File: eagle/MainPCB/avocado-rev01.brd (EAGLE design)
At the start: 100 x 60 mm, 85 parts, among them J1 10118194-0001LF, J2 CON-DSUB-15-VGA, J3 0475710001, P2 CONNECTOR-15686115148922, U1 V3S, U2 AP65111A, U3 AP65111A, U4 AP65111A

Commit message: updated i2c
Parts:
- removed R31: 2k, resistor:R0603
- R27: value (none) -> 2k
- moved R27 2.00 mm to (69.0, 37.0)
- moved R28 2.00 mm to (69.0, 39.0)
- moved R29 2.00 mm to (69.0, 41.0)
- moved R30 2.00 mm to (69.0, 43.0)
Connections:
- net N$49: no longer R28.2
- net N$50: now also R28.2; no longer R29.2
- net N$51: now also R29.2; no longer R30.2
- net N$52: now also R30.2; no longer R31.2
- net N$63: no longer R31.1
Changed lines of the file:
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@@
 <attribute name="X" value="X" x="38" y="58" size="1.778" layer="27" rot="R270" display="off"/>
 </element>
-<element name="R27" library="resistor" library_urn="urn:adsk.eagle:library:348" package="R0603" package3d_urn="urn:adsk.eagle:package:26057/1" value="" x="69" y="35" smashed="yes" rot="R180">
-<attribute name="NAME" x="74.635" y="35.365" size="1.27" layer="25" rot="R180"/>
-<attribute name="VALUE" x="69.635" y="36.905" size="1.27" layer="27" rot="R180"/>
-</element>
-<element name="R28" library="resistor" library_urn="urn:adsk.eagle:library:348" package="R0603" package3d_urn="urn:adsk.eagle:package:26057/1" value="2k" x="69" y="37" smashed="yes" rot="R180">
+<element name="R27" library="resistor" library_urn="urn:adsk.eagle:library:348" package="R0603" package3d_urn="urn:adsk.eagle:package:26057/1" value="2k" x="69" y="37" smashed="yes" rot="R180">
 <attribute name="NAME" x="74.635" y="37.365" size="1.27" layer="25" rot="R180"/>
 <attribute name="VALUE" x="69.635" y="38.905" size="1.27" layer="27" rot="R180"/>
 </element>
-<element name="R29" library="resistor" library_urn="urn:adsk.eagle:library:348" package="R0603" package3d_urn="urn:adsk.eagle:package:26057/1" value="2k" x="69" y="39" smashed="yes" rot="R180">
+<element name="R28" library="resistor" library_urn="urn:adsk.eagle:library:348" package="R0603" package3d_urn="urn:adsk.eagle:package:26057/1" value="2k" x="69" y="39" smashed="yes" rot="R180">
 <attribute name="NAME" x="74.635" y="39.365" size="1.27" layer="25" rot="R180"/>
 <attribute name="VALUE" x="69.635" y="40.905" size="1.27" layer="27" rot="R180"/>
 </element>
-<element name="R30" library="resistor" library_urn="urn:adsk.eagle:library:348" package="R0603" package3d_urn="urn:adsk.eagle:package:26057/1" value="2k" x="69" y="41" smashed="yes" rot="R180">
+<element name="R29" library="resistor" library_urn="urn:adsk.eagle:library:348" package="R0603" package3d_urn="urn:adsk.eagle:package:26057/1" value="2k" x="69" y="41" smashed="yes" rot="R180">
 <attribute name="NAME" x="74.635" y="41.365" size="1.27" layer="25" rot="R180"/>
 <attribute name="VALUE" x="69.635" y="42.905" size="1.27" layer="27" rot="R180"/>
 </element>
-<element name="R31" library="resistor" library_urn="urn:adsk.eagle:library:348" package="R0603" package3d_urn="urn:adsk.eagle:package:26057/1" value="2k" x="69" y="43" smashed="yes" rot="R180">
+<element name="R30" library="resistor" library_urn="urn:adsk.eagle:library:348" package="R0603" package3d_urn="urn:adsk.eagle:package:26057/1" value="2k" x="69" y="43" smashed="yes" rot="R180">
 <attribute name="NAME" x="74.635" y="43.365" size="1.27" layer="25" rot="R180"/>
 <attribute name="VALUE" x="69.635" y="44.905" size="1.27" layer="27" rot="R180"/>
@@
 <contactref element="TP5" pad="1"/>
 <contactref element="R27" pad="2"/>
-<contactref element="R28" pad="2"/>
 <wire x1="56.363959375" y1="34.384059375" x2="56" y2="58" width="0" layer="19" extent="1-1"/>
-<wire x1="68.15" y1="35" x2="56.363959375" y2="34.384059375" width="0" layer="19" extent="1-1"/>
-<wire x1="68.15" y1="37" x2="68.15" y2="35" width="0" layer="19" extent="1-1"/>
+<wire x1="68.15" y1="37" x2="56.363959375" y2="34.384059375" width="0" layer="19" extent="1-1"/>
 </signal>
 <signal name="N$50">
 <contactref element="U1" pad="46"/>
 <contactref element="TP6" pad="1"/>
-<contactref element="R29" pad="2"/>
+<contactref element="R28" pad="2"/>
 <wire x1="56.081115625" y1="34.666903125" x2="54" y2="58" width="0" layer="19" extent="1-1"/>
 <wire x1="68.15" y1="39" x2="56.081115625" y2="34.666903125" width="0" layer="19" extent="1-1"/>
@@
 <contactref element="U1" pad="48"/>
 <contactref element="TP7" pad="1"/>
-<contactref element="R30" pad="2"/>
+<contactref element="R29" pad="2"/>
 <wire x1="55.51543125" y1="35.2325875" x2="52" y2="58" width="0" layer="19" extent="1-1"/>
 <wire x1="68.15" y1="41" x2="55.51543125" y2="35.2325875" width="0" layer="19" extent="1-1"/>
@@
 <contactref element="U1" pad="49"/>
 <contactref element="TP8" pad="1"/>
-<contactref element="R31" pad="2"/>
+<contactref element="R30" pad="2"/>
 <wire x1="55.2325875" y1="35.51543125" x2="50" y2="58" width="0" layer="19" extent="1-1"/>
 <wire x1="68.15" y1="43" x2="55.2325875" y2="35.51543125" width="0" layer="19" extent="1-1"/>
@@
 <signal name="N$63">
 <contactref element="R27" pad="1"/>
+<contactref element="R30" pad="1"/>
 <contactref element="R28" pad="1"/>
-<contactref element="R31" pad="1"/>
 <contactref element="R29" pad="1"/>
-<contactref element="R30" pad="1"/>
 <wire x1="69.85" y1="41" x2="69.85" y2="43" width="0" layer="19" extent="1-1"/>
 <wire x1="69.85" y1="39" x2="69.85" y2="41" width="0" layer="19" extent="1-1"/>
 <wire x1="69.85" y1="37" x2="69.85" y2="39" width="0" layer="19" extent="1-1"/>
-<wire x1="69.85" y1="35" x2="69.85" y2="37" width="0" layer="19" extent="1-1"/>
 </signal>
 </signals>

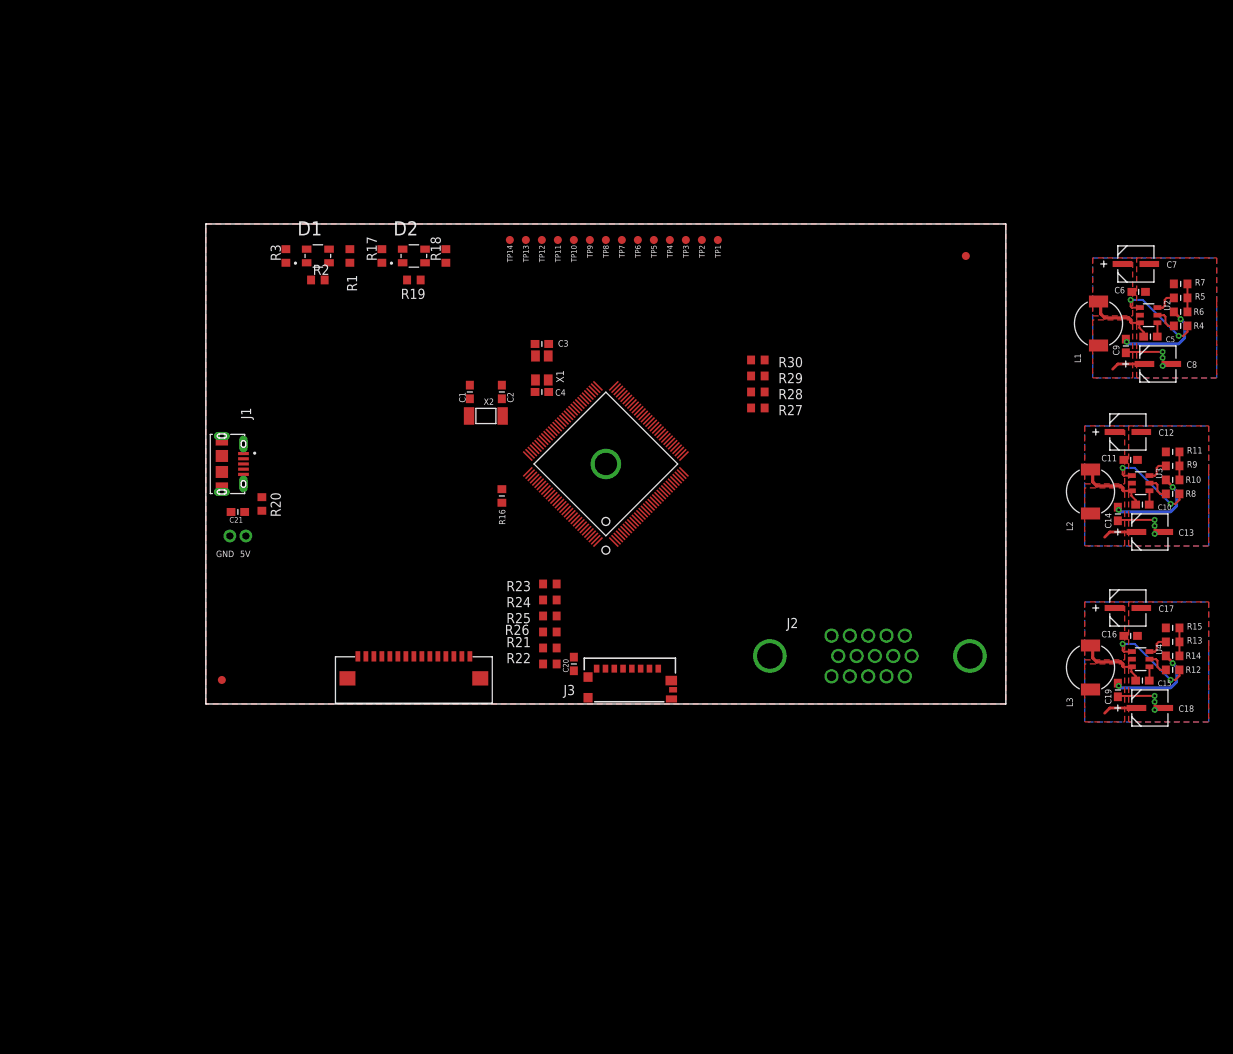
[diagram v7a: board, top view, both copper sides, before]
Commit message: connected psu in schem
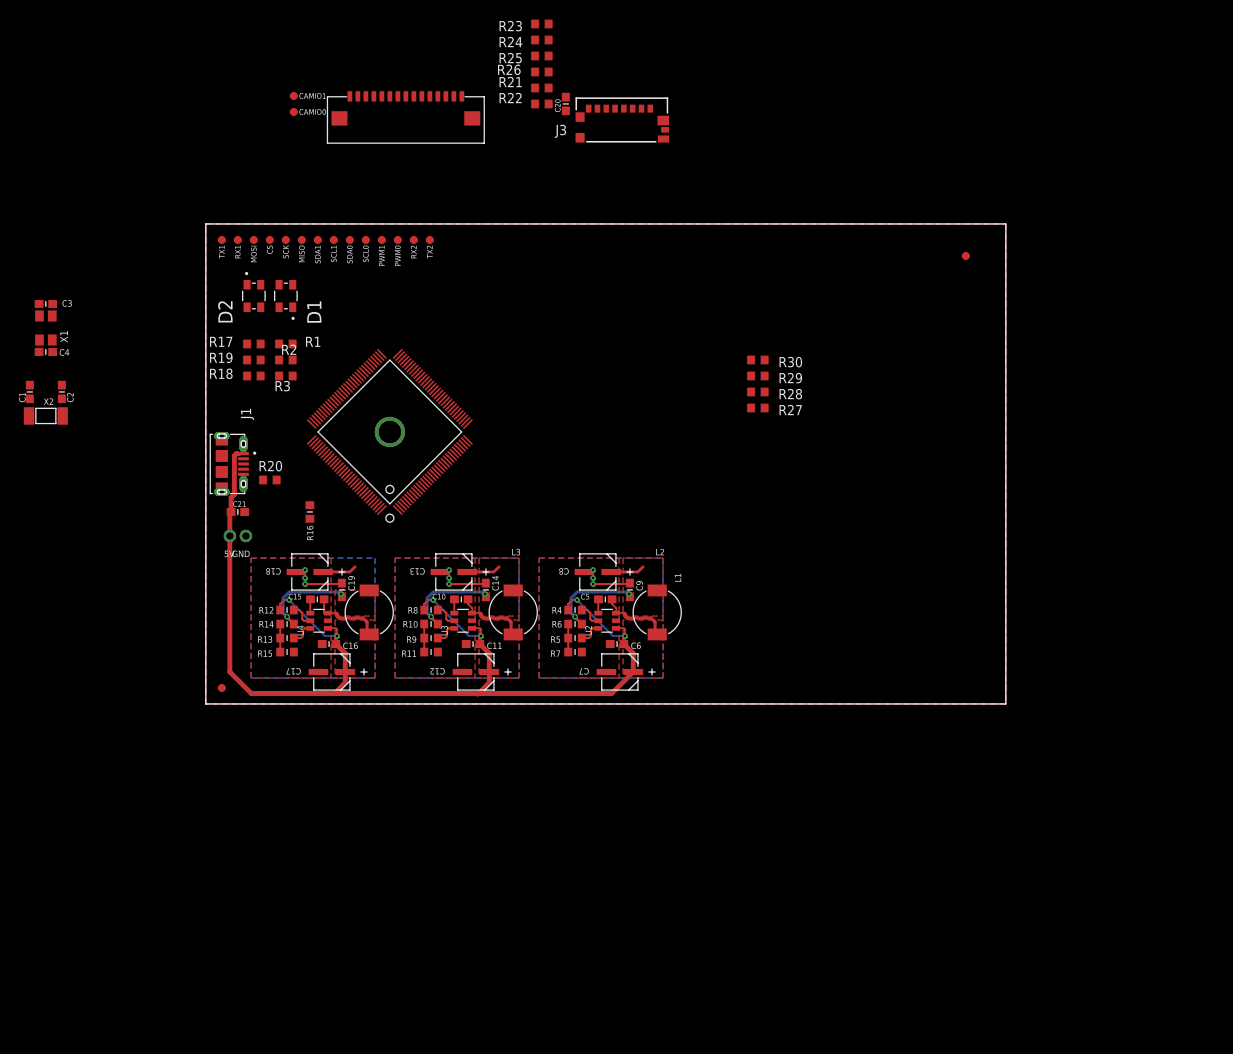
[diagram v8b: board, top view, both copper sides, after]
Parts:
- removed J2: CON-DSUB-15-VGA, m-pad-2.1:181-015-212-171
- removed TP1, TP10, TP11, TP12, TP13, TP14, TP2, TP3, TP4, TP5, TP6, TP7, TP8, TP9: TEST_TESTPOINT, marius:TEST_TESTPOINT
- added CAMIO0, CAMIO1, CS, MISO, MOSI, PWM0, PWM1, RX1, RX2, SCK, SCL0, SCL1, SDA0, SDA1, TX1, TX2: TEST_TESTPOINT, marius:TEST_TESTPOINT
- moved R12 111.0 mm to (10.2, 11.7), turned to 180 degrees
- moved R14 110.8 mm to (10.2, 9.99), turned to 180 degrees
- moved R15 110.7 mm to (10.2, 6.49), turned to 0 degrees
- moved R13 110.7 mm to (10.2, 8.24), turned to 0 degrees
- moved C18 106.4 mm to (13.0, 16.5), turned to 180 degrees
- moved C15 103.6 mm to (13.9, 13.1), turned to 0 degrees
- moved U4 102.8 mm to (14.2, 10.4), turned to 90 degrees
- moved C16 100.2 mm to (15.4, 7.49), turned to 180 degrees
- moved C17 99.8 mm to (15.8, 4.00), turned to 180 degrees
- moved C19 97.8 mm to (17.0, 14.2), turned to 90 degrees
- moved R11 96.0 mm to (28.1, 6.49), turned to 0 degrees
- moved R9 95.2 mm to (28.1, 8.24), turned to 0 degrees
- moved R10 94.4 mm to (28.1, 9.99), turned to 180 degrees
- moved R8 93.8 mm to (28.1, 11.7), turned to 180 degrees
- moved L3 90.4 mm to (20.4, 11.4), turned to 90 degrees
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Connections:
- removed net N$26: R2.1
- removed net N$32: R1.1
- removed net N$33: R17.1
- removed net N$35: R18.1
- removed net N$36: R19.1
- removed net N$37: U1.5
- removed net N$38: U1.4
- removed net N$39: U1.3
- removed net N$51: R29.2, TP7.1, U1.48
- removed net N$52: R30.2, TP8.1, U1.49
- removed net N$7: U1.77
- removed net N$8: U1.78
- removed net VIN: C11.1, C12.1, C16.1, C17.1, C6.1, C7.1, R12.2, R4.2, R8.2, U2.1, U3.1, U4.1
- new net CAM_IO0: CAMIO0.1, P2.11
- new net CAM_IO1: CAMIO1.1, P2.12
- new net LED0: R18.1, U1.4
- new net LED1: R19.1, U1.5
- new net LED2: R17.1, U1.3
- new net LED3: R1.1, U1.78
- new net LED4: R2.1, U1.77
- new net N$65: P2.2, U1.82
- new net N$66: P2.3, U1.81
- new net N$68: P2.5, U1.84
- new net N$69: P2.6, U1.83
- new net N$70: P2.8, U1.87
- new net N$71: P2.15
- new net N$72: P2.9, U1.86
- new net SCL: P2.13, R29.2, SCL1.1, U1.48
- new net SDA: P2.14, R30.2, SDA1.1, U1.49
- net GND: now also P2.1, P2.10, P2.4, P2.7
- net N$47: now also TX2.1; no longer TP1.1
- net N$48: now also RX2.1; no longer TP2.1
- net N$49: now also SCL0.1; no longer TP5.1
- net N$50: now also SDA0.1; no longer TP6.1
- net N$53: now also MISO.1; no longer TP9.1
- net N$54: now also SCK.1; no longer TP10.1
- net N$55: now also CS.1; no longer TP11.1
- net N$56: now also MOSI.1; no longer TP12.1
- net N$57: now also PWM0.1; no longer TP3.1
- net N$58: now also PWM1.1; no longer TP4.1
- net N$59: now also TX1.1; no longer TP14.1
- net N$60: now also RX1.1; no longer TP13.1
- net VCC: now also C11.1, C12.1, C16.1, C17.1, C6.1, C7.1, R12.2, R4.2, R8.2, U2.1, U3.1, U4.1
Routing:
- net VCC: track 0.00 -> 187.4 mm, vias 0 -> 6
- net VIN: track 35.9 -> 0.00 mm, vias 6 -> 0
